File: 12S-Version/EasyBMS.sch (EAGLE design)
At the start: 157 parts, among them IC1 LM2596S-5.0_NOPB, IC2 LTC6811IG-1#PBF, Q10 BSS84LT1G, Q11 BSS84LT1G, Q12 BSS84LT1G, Q13 BSS84LT1G, Q2 BSS84LT1G, Q3 BSS84LT1G, Q4 BSS84LT1G, Q5 BSS84LT1G, Q6 BSS84LT1G, Q7 BSS84LT1G, Q8 BSS84LT1G, Q9 BSS84LT1G

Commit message: GND seperated in GND2 and GND
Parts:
- removed JP10, JP11: (no value), pinhead:PINHD-1X2
- removed JP9: (no value), pinhead:PINHD-1X5
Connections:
- net +5V: no longer JP9.1, JP9.2
- net C1-: no longer JP7.15_TOTAL-
- net GND: now also JP7.15_TOTAL-, LED1.C, LED2.C, LED3.C, LED4.C, U$2.GND; no longer C1.2, C19.2, C20.1, C22.2, C23.-, C4.2, C5.2, IC2.ISOMD, IC2.V-_1, IC2.V-_2, JP10.1, JP10.2, JP11.1, JP11.2, JP9.4, JP9.5, R13.2, R17.1, R57.1, R58.1
- net GND2: now also C1.2, C19.2, C20.1, C22.2, C23.-, C4.2, C5.2, IC2.ISOMD, IC2.V-_1, IC2.V-_2, R13.2, R17.1, R57.1, R58.1; no longer LED1.C, LED2.C, LED3.C, LED4.C, U$2.GND
- net ISIGNAL: no longer JP9.3

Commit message: reviewed and new pcb version
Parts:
- added C3: 100n, rcl:C-EUC0402
- R13, R18: value C1017 -> C370100; device rcl:R-EU_R0805 -> rcl:R-EU_R1206
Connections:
- net GND: now also C3.2
- net GND2: now also C3.1

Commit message: comments to Digital pins added
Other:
- note added: "Balance active"
- note added: "LED builtin - Heartbeat?"
- note added: "SPI ok/lost"
- note added: "Used for Display control in Future"
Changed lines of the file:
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@@
 <sheet>
 <plain>
+<text x="80.645" y="345.44" size="1.778" layer="91">SPI ok/lost</text>
+<text x="80.645" y="335.28" size="1.778" layer="91">Balance active</text>
+<text x="80.645" y="314.96" size="1.778" layer="91">LED builtin - Heartbeat?</text>
+<text x="80.645" y="325.12" size="1.778" layer="91">Used for Display control in Future</text>
 </plain>
 <instances>

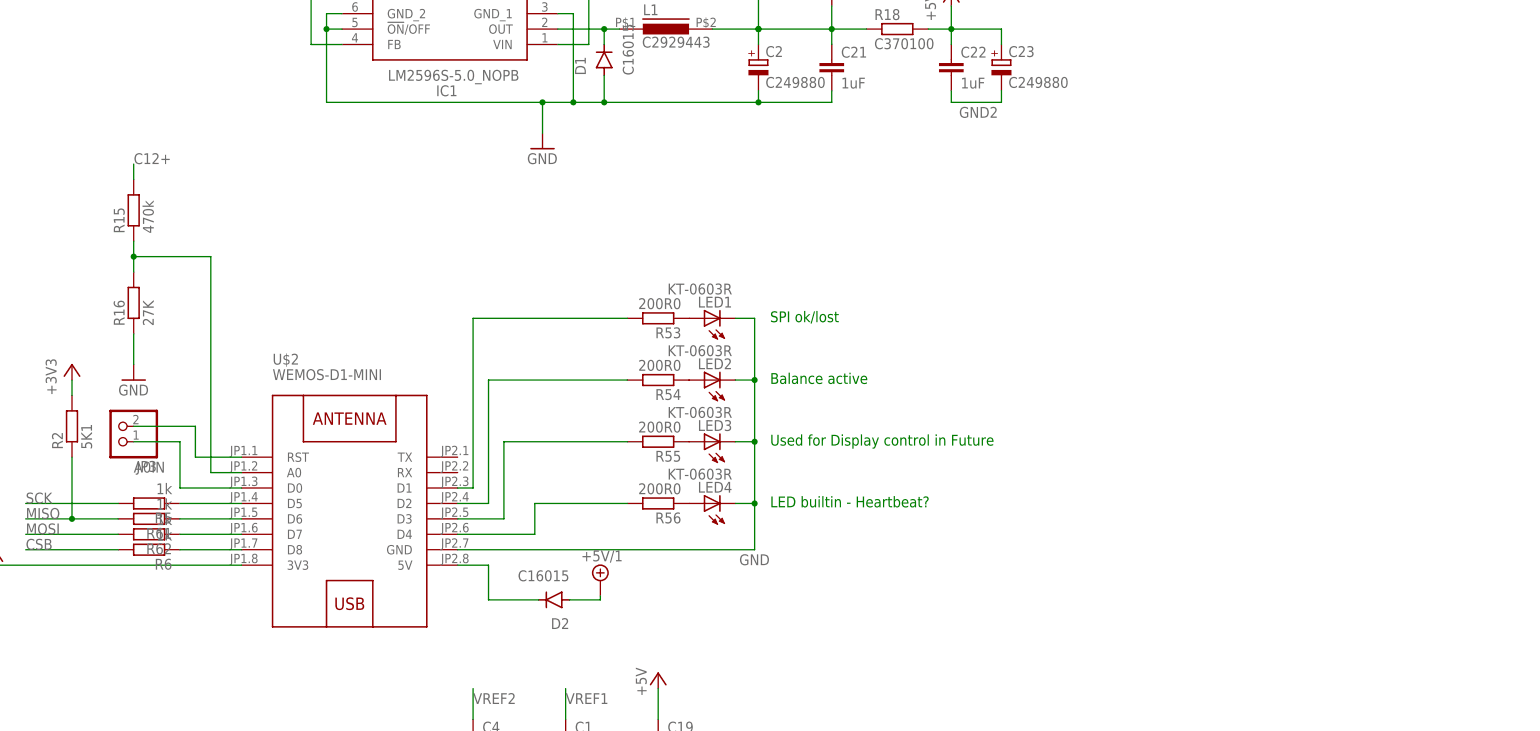
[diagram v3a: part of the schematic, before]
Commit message: pinheader for display added
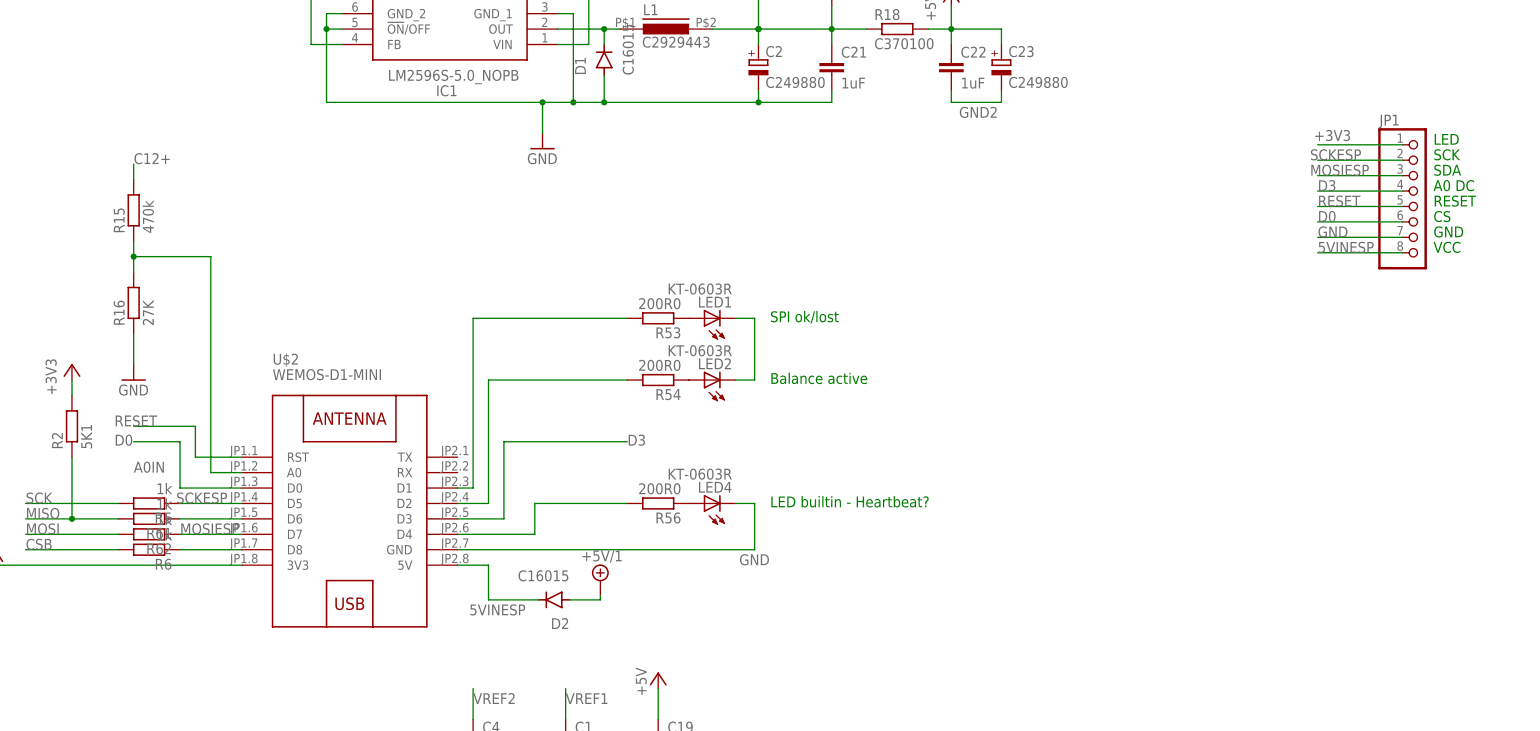
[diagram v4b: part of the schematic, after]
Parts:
- removed JP3: (no value), pinhead_own:PINHD-1X2
- removed LED3: KT-0603R, led:LEDCHIPLED_0603
- removed R55: 200R0, rcl:R-EU_R0603
- added JP1: (no value), pinhead:PINHD-1X8
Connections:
- removed net N$119: R62.1, U$2.D7
- removed net N$120: R55.2, U$2.D3
- removed net N$25: D2.C, U$2.5V
- removed net N$5: JP3.2, U$2.RST
- removed net N$6: JP3.1, U$2.D0
- removed net N$7: R5.1, U$2.D5
- new net 5VINESP: D2.C, JP1.8, U$2.5V
- new net D0: JP1.6, U$2.D0
- new net D3: JP1.4, U$2.D3
- new net MOSIESP: JP1.3, R62.1, U$2.D7
- new net RESET: JP1.5, U$2.RST
- new net SCKESP: JP1.2, R5.1, U$2.D5
- net +3V3: now also JP1.1
- net GND: now also JP1.7; no longer LED1.C, LED2.C, LED3.C
- net N$3: now also LED1.C, LED2.C; no longer LED3.A, R55.1
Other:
- note added: "A0 DC"
- note added: "CS"
- note added: "GND"
- note added: "LED"
- note added: "RESET"
- note added: "SCK"
- note added: "SDA"
- note added: "VCC"
- note removed: "Used for Display control in Future"

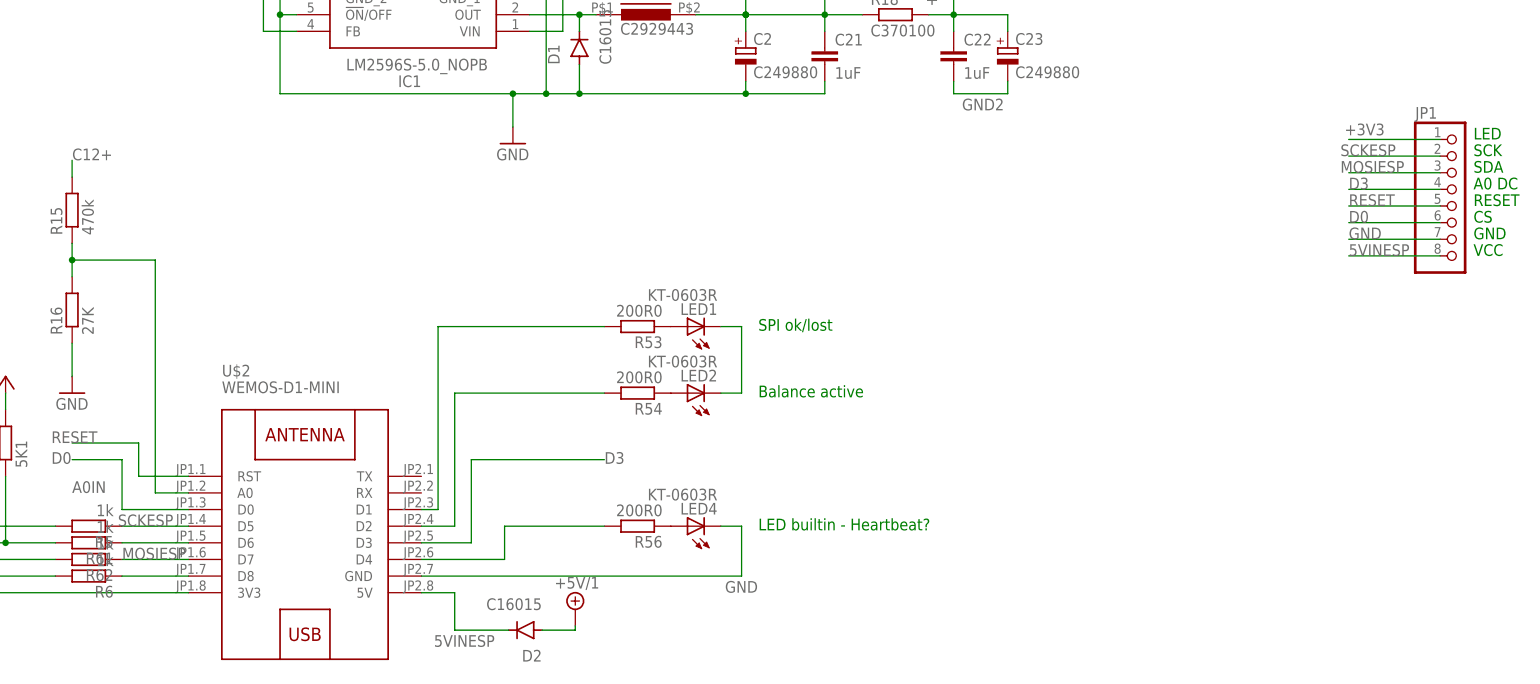
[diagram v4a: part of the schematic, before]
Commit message: moved display connector
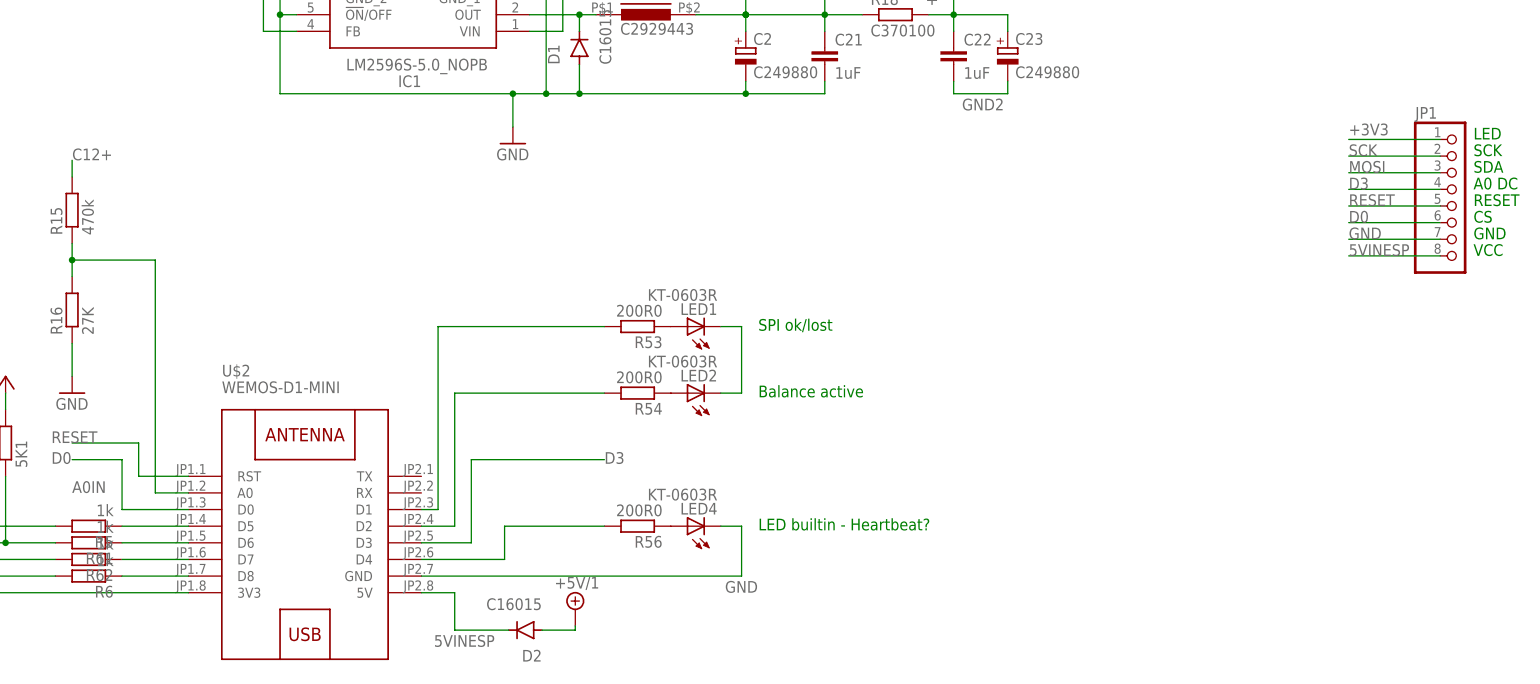
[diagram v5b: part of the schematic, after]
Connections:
- net MOSI: now also JP1.3
- net MOSIESP: no longer JP1.3
- net SCK: now also JP1.2
- net SCKESP: no longer JP1.2
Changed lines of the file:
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@@
 <pinref part="IC2" gate="G$1" pin="SDI_(NC)"/>
+</segment>
+<segment>
+<pinref part="JP1" gate="A" pin="3"/>
+<wire x1="184.785" y1="369.57" x2="170.815" y2="369.57" width="0.1524" layer="91"/>
+<label x="170.815" y="369.57" size="1.778" layer="95"/>
 </segment>
 </net>
@@
 <pinref part="R62" gate="G$1" pin="1"/>
 <wire x1="-6.35" y1="310.515" x2="-16.51" y2="310.515" width="0.1524" layer="91"/>
-<label x="-16.51" y="310.515" size="1.778" layer="95"/>
-</segment>
-<segment>
-<pinref part="JP1" gate="A" pin="3"/>
-<wire x1="184.785" y1="369.57" x2="170.815" y2="369.57" width="0.1524" layer="91"/>
-<label x="169.545" y="369.57" size="1.778" layer="95"/>
 </segment>
 </net>
@@
 <wire x1="-26.67" y1="315.595" x2="-41.91" y2="315.595" width="0.1524" layer="91"/>
 <label x="-41.91" y="315.595" size="1.778" layer="95"/>
+</segment>
+<segment>
+<pinref part="JP1" gate="A" pin="2"/>
+<wire x1="184.785" y1="372.11" x2="170.815" y2="372.11" width="0.1524" layer="91"/>
+<label x="170.815" y="372.11" size="1.778" layer="95"/>
 </segment>
 </net>
@@
 <pinref part="R5" gate="G$1" pin="1"/>
 <wire x1="-6.35" y1="315.595" x2="-16.51" y2="315.595" width="0.1524" layer="91"/>
-<label x="-17.145" y="315.595" size="1.778" layer="95"/>
-</segment>
-<segment>
-<pinref part="JP1" gate="A" pin="2"/>
-<wire x1="184.785" y1="372.11" x2="170.815" y2="372.11" width="0.1524" layer="91"/>
-<label x="169.545" y="372.11" size="1.778" layer="95"/>
 </segment>
 </net>
@@
 <pinref part="JP1" gate="A" pin="1"/>
 <wire x1="184.785" y1="374.65" x2="170.815" y2="374.65" width="0.1524" layer="91"/>
-<label x="170.18" y="375.285" size="1.778" layer="95"/>
-</segment>
-</net>
+<label x="170.815" y="375.285" size="1.778" layer="95"/>
+</segment>
+</net>

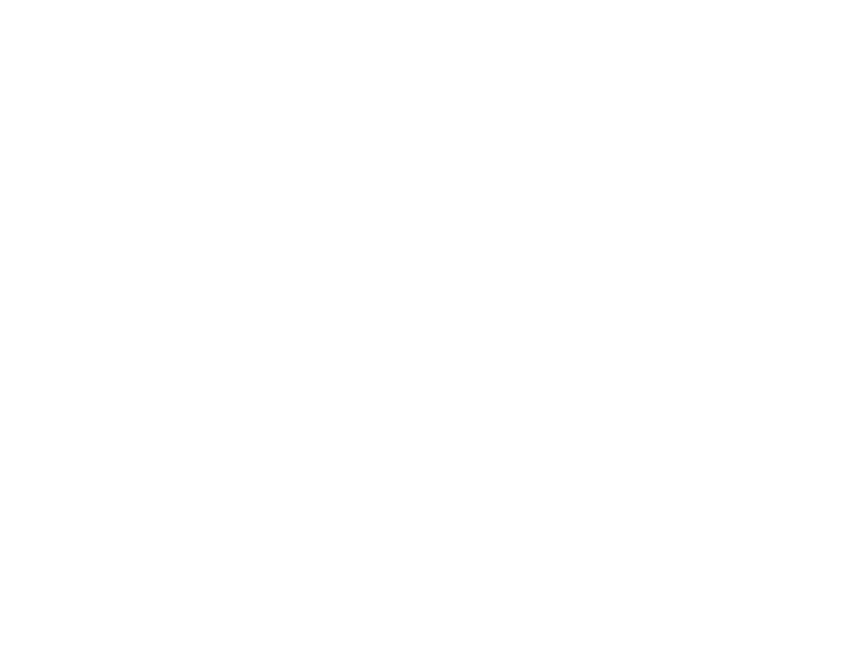
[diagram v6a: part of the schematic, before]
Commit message: level shifter base design added
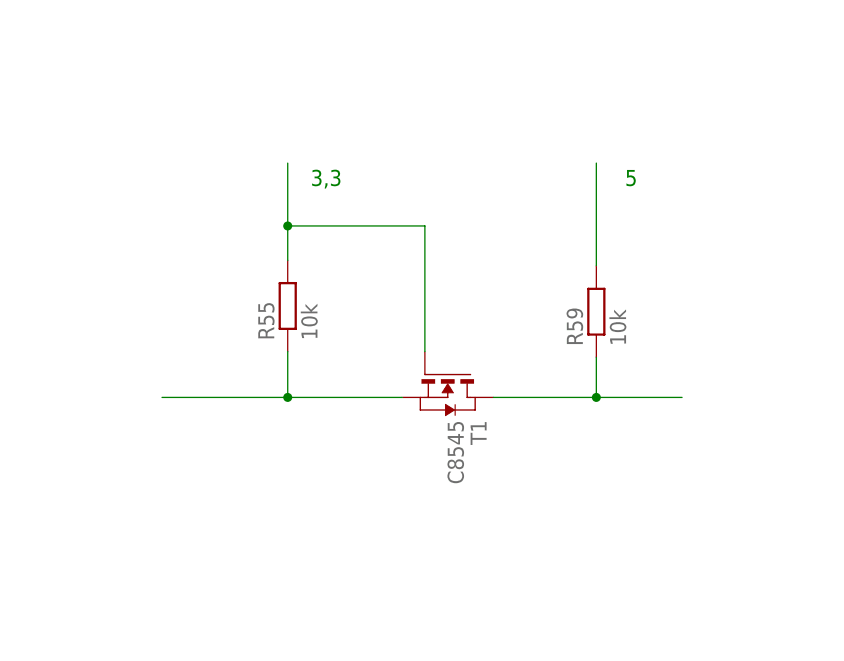
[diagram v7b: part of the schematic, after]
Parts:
- added R55, R59: 10k, rcl:R-EU_R0603
- added T1: C8545, zetex:NMOSSOT23
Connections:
- new net N$18: R59.2
- new net N$5: R55.2, T1.G
- new net N$6: R55.1, T1.S
- new net N$7: R59.1, T1.D
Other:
- note added: "3,3"
- note added: "5"
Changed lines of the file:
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@@
 <part name="GND1" library="supply1" library_urn="urn:adsk.eagle:library:371" deviceset="GND" device=""/>
 <part name="JP1" library="pinhead" library_urn="urn:adsk.eagle:library:325" deviceset="PINHD-1X8" device="" package3d_urn="urn:adsk.eagle:package:22409/2"/>
+<part name="T1" library="zetex" library_urn="urn:adsk.eagle:library:418" deviceset="NMOSSOT23" device="" package3d_urn="urn:adsk.eagle:package:30981/1" value="C8545"/>
+<part name="R55" library="rcl" library_urn="urn:adsk.eagle:library:334" deviceset="R-EU_" device="R0603" package3d_urn="urn:adsk.eagle:package:23555/3" value="10k"/>
+<part name="R59" library="rcl" library_urn="urn:adsk.eagle:library:334" deviceset="R-EU_" device="R0603" package3d_urn="urn:adsk.eagle:package:23555/3" value="10k"/>
 </parts>
 <sheets>
@@
 <text x="189.865" y="359.41" size="1.778" layer="91">GND</text>
 <text x="189.865" y="356.87" size="1.778" layer="91">VCC</text>
+<text x="-2.54" y="232.41" size="1.778" layer="91">3,3</text>
+<text x="32.385" y="232.41" size="1.778" layer="91">5</text>
 </plain>
 <instances>
@@
 <attribute name="NAME" x="180.975" y="377.825" size="1.778" layer="95"/>
 <attribute name="VALUE" x="180.975" y="351.79" size="1.778" layer="96"/>
+</instance>
+<instance part="T1" gate="A" x="12.7" y="208.915" smashed="yes" rot="R270">
+<attribute name="VALUE" x="12.7" y="206.375" size="1.778" layer="96" rot="R270"/>
+<attribute name="NAME" x="15.24" y="206.375" size="1.778" layer="95" rot="R270"/>
+</instance>
+<instance part="R55" gate="G$1" x="-5.08" y="219.075" smashed="yes" rot="R90">
+<attribute name="NAME" x="-6.5786" y="215.265" size="1.778" layer="95" rot="R90"/>
+<attribute name="VALUE" x="-1.778" y="215.265" size="1.778" layer="96" rot="R90"/>
+</instance>
+<instance part="R59" gate="G$1" x="29.21" y="218.44" smashed="yes" rot="R90">
+<attribute name="NAME" x="27.7114" y="214.63" size="1.778" layer="95" rot="R90"/>
+<attribute name="VALUE" x="32.512" y="214.63" size="1.778" layer="96" rot="R90"/>
 </instance>
 </instances>
@@
 </segment>
 </net>
+<net name="N$5" class="0">
+<segment>
+<pinref part="R55" gate="G$1" pin="2"/>
+<wire x1="-5.08" y1="224.155" x2="-5.08" y2="227.965" width="0.1524" layer="91"/>
+<wire x1="-5.08" y1="227.965" x2="-5.08" y2="234.95" width="0.1524" layer="91"/>
+<pinref part="T1" gate="A" pin="G"/>
+<wire x1="10.16" y1="213.995" x2="10.16" y2="227.965" width="0.1524" layer="91"/>
+<wire x1="10.16" y1="227.965" x2="-5.08" y2="227.965" width="0.1524" layer="91"/>
+<junction x="-5.08" y="227.965"/>
+</segment>
+</net>
+<net name="N$6" class="0">
+<segment>
+<pinref part="R55" gate="G$1" pin="1"/>
+<pinref part="T1" gate="A" pin="S"/>
+<wire x1="-5.08" y1="213.995" x2="-5.08" y2="208.915" width="0.1524" layer="91"/>
+<wire x1="-5.08" y1="208.915" x2="7.62" y2="208.915" width="0.1524" layer="91"/>
+<wire x1="-5.08" y1="208.915" x2="-19.05" y2="208.915" width="0.1524" layer="91"/>
+<junction x="-5.08" y="208.915"/>
+</segment>
+</net>
+<net name="N$7" class="0">
+<segment>
+<pinref part="T1" gate="A" pin="D"/>
+<pinref part="R59" gate="G$1" pin="1"/>
+<wire x1="17.78" y1="208.915" x2="29.21" y2="208.915" width="0.1524" layer="91"/>
+<wire x1="29.21" y1="208.915" x2="29.21" y2="213.36" width="0.1524" layer="91"/>
+<wire x1="29.21" y1="208.915" x2="38.735" y2="208.915" width="0.1524" layer="91"/>
+<junction x="29.21" y="208.915"/>
+</segment>
+</net>
+<net name="N$18" class="0">
+<segment>
+<pinref part="R59" gate="G$1" pin="2"/>
+<wire x1="29.21" y1="223.52" x2="29.21" y2="234.95" width="0.1524" layer="91"/>
+</segment>
+</net>
